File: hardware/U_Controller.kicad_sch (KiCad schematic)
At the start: 14 parts, among them J7001 USB_C_Receptacle_USB2.0_14P, SW7001 SW_Wuerth_450301014042, U7001 STM32C031K6Tx, U7002 STM32C071RBT6, U7003 USBLC6-2SC6, Y7001 Crystal_GND24

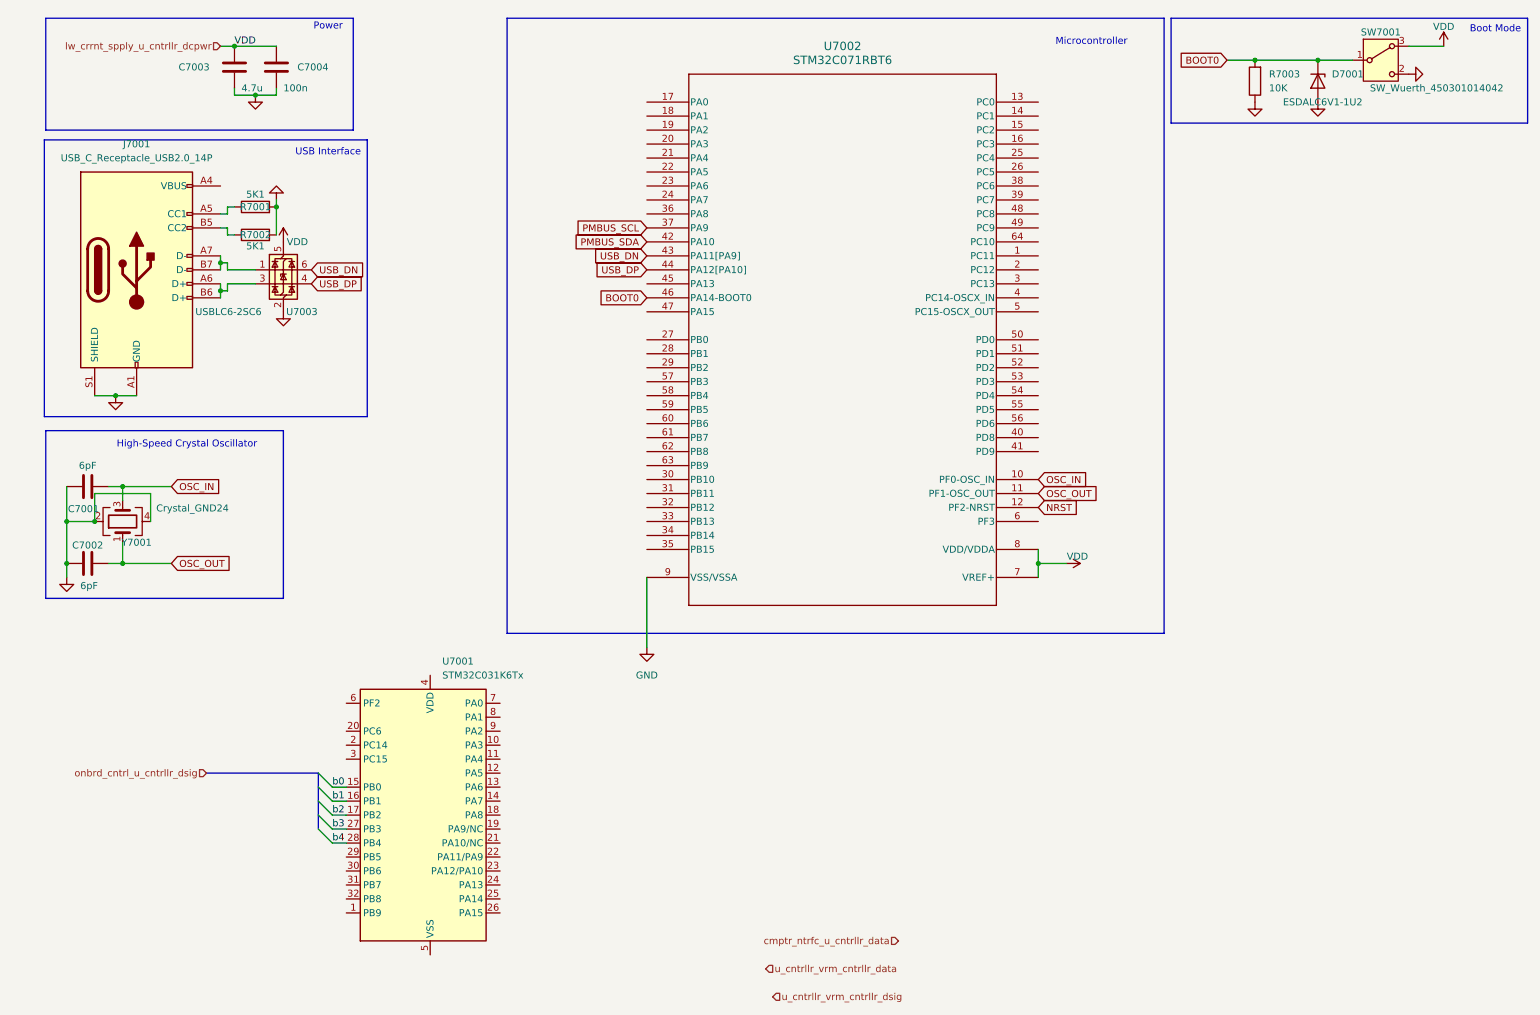
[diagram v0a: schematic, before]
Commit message: refactor(schematic): proper pin mappings
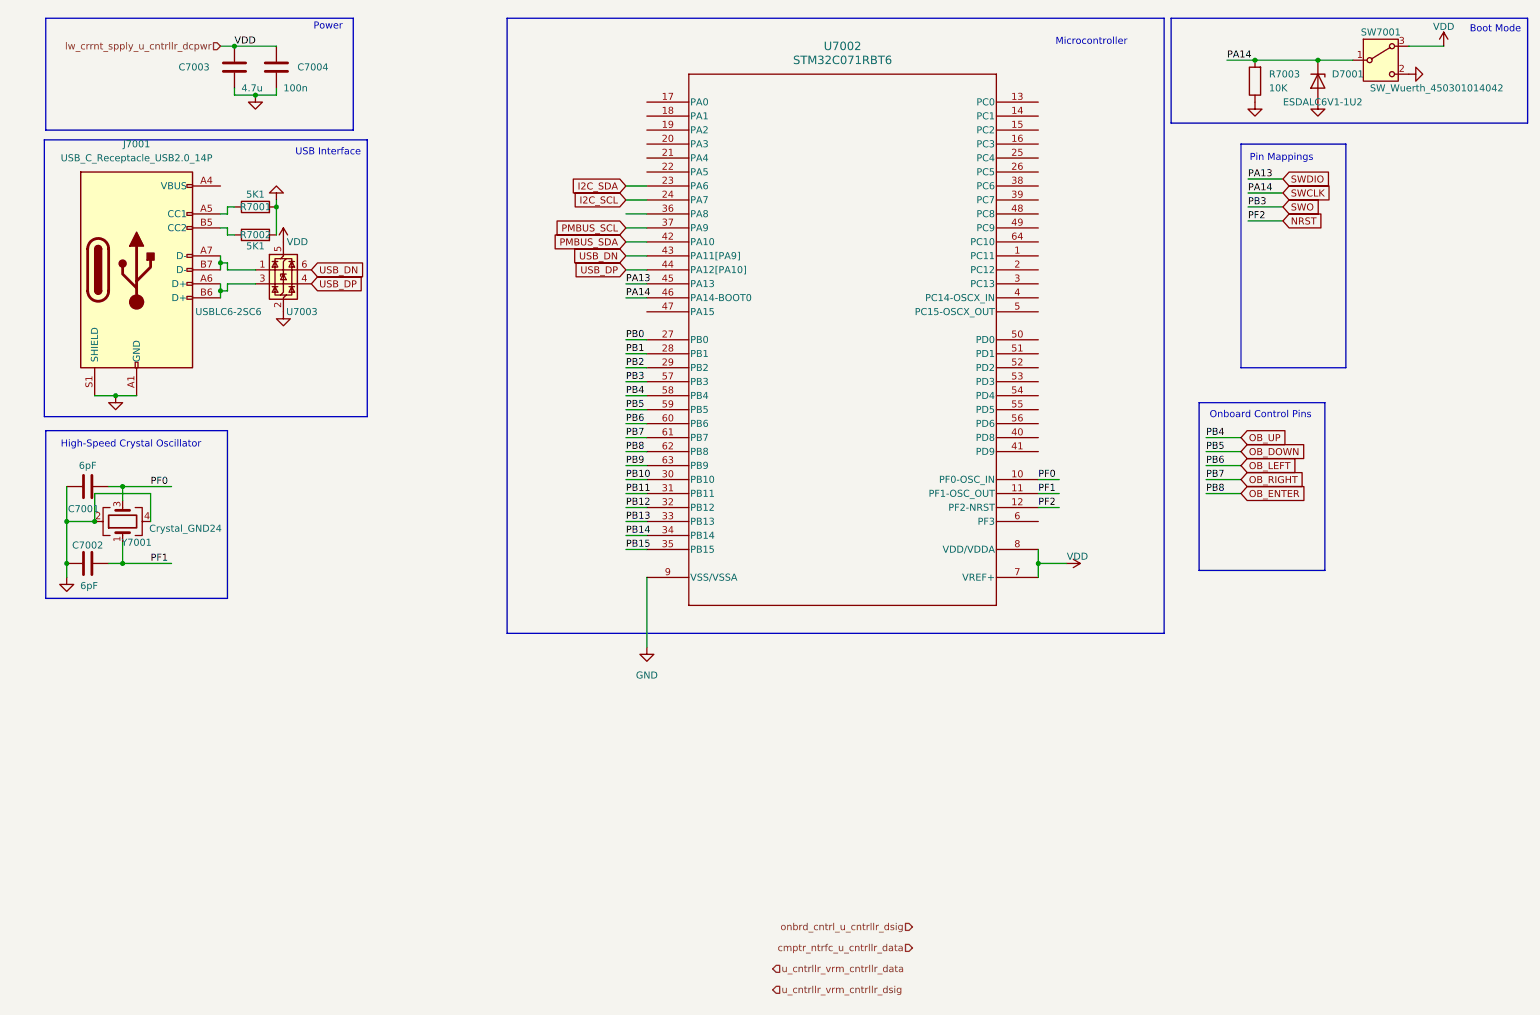
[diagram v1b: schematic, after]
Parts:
- removed U7001: STM32C031K6Tx, Package_QFP:LQFP-32_7x7mm_P0.8mm, symbol MCU_ST_STM32C0:STM32C031K6Tx
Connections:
- net I2C_SDA: now reaches U7002.23 (PA6)
- net I2C_SCL: now reaches U7002.24 (PA7)
- net PB0: now reaches U7002.27 (PB0)
- net PB1: now reaches U7002.28 (PB1)
- net PB2: now reaches U7002.29 (PB2)
- net PB10: now reaches U7002.30 (PB10)
- net PB11: now reaches U7002.31 (PB11)
- net PB12: now reaches U7002.32 (PB12)
- net PB13: now reaches U7002.33 (PB13)
- net PB14: now reaches U7002.34 (PB14)
- net PB15: now reaches U7002.35 (PB15)
- net SWDIO: now reaches U7002.45 (PA13)
- net SWO: now reaches U7002.57 (PB3)
- net OB_UP: now reaches U7002.58 (PB4)
- net OB_DOWN: now reaches U7002.59 (PB5)
- net OB_LEFT: now reaches U7002.60 (PB6)
- net OB_RIGHT: now reaches U7002.61 (PB7)
- net OB_ENTER: now reaches U7002.62 (PB8)
- net PB9: now reaches U7002.63 (PB9)
- net BOOT0 renamed SWCLK
- net OSC_IN renamed PF0
- net OSC_OUT renamed PF1
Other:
- note added: "Onboard Control Pins"
- note added: "Pin Mappings"

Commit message: feat(schematic): SWD connector
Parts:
- added J7002: Conn_ARM_JTAG_SWD_10, symbol Connector:Conn_ARM_JTAG_SWD_10
- added R7004, R7005: 100k, symbol Device:R
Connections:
- net GND: now also J7002.3 (GND), J7002.5 (GND), J7002.9 (GNDDetect), R7005.2
- net NRST: now also J7002.10 (~{RESET})
- net SWCLK: now also J7002.2 (SWDIO/TMS), R7005.1
- net SWDIO: now also J7002.4 (SWCLK/TCK), R7004.2
- net SWO: now also J7002.6 (SWO/TDO)
- net VDD: now also J7002.1 (VTref), R7004.1
- net 12V_CUR_SENS: now reaches U7002.17 (PA0)
- net 12V_VOL_SENS: now reaches U7002.18 (PA1)
- no-connect marks 0 -> 1
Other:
- note added: "12V Supply Pins"
- note added: "SWD Connector"

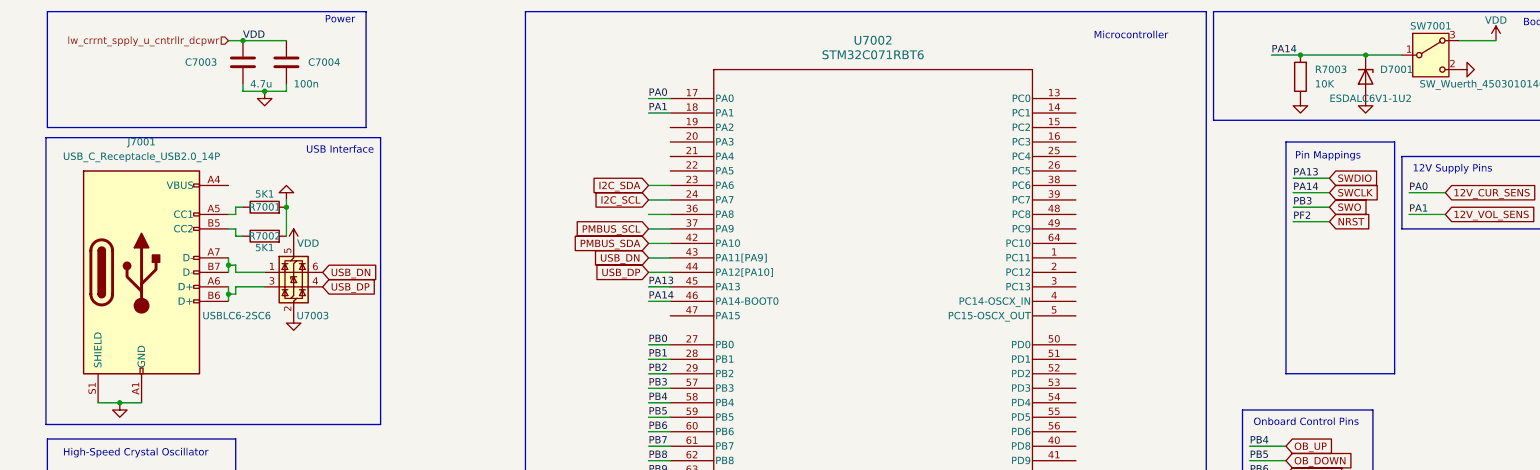
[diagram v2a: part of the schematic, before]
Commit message: chore(schematic): add footprints and datasheets for microcontroller
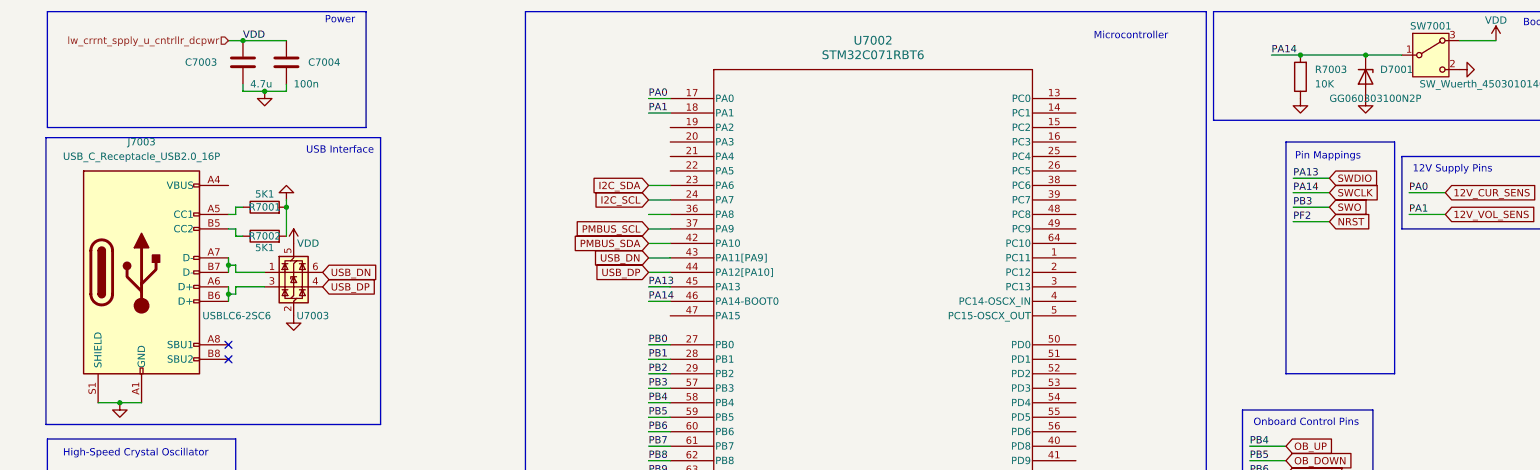
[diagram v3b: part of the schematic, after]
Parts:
- removed J7001: USB_C_Receptacle_USB2.0_14P, symbol Connector:USB_C_Receptacle_USB2.0_14P
- added J7003: USB_C_Receptacle_USB2.0_16P, work:12402012E212A_AMP, symbol Connector:USB_C_Receptacle_USB2.0_16P
- C7001, C7002, C7003, C7004: footprint (none) -> Capacitor_SMD:C_0805_2012Metric
- D7001: value ESDALC6V1-1U2 -> GG060303100N2P; footprint (none) -> Diode_SMD:D_0603_1608Metric
- J7002: footprint (none) -> work:CNC_3221-10-0100-00
- R7001, R7002, R7003, R7004, R7005: footprint (none) -> Resistor_SMD:R_0805_2012Metric
- Y7001: footprint (none) -> Crystal:Crystal_SMD_Abracon_ABM10-4Pin_2.5x2.0mm
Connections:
- net GND: now also J7003.A1 (GND), J7003.A12 (GND), J7003.B1 (GND), J7003.B12 (GND), J7003.S1 (SHIELD)
- net at R7002.1: now also J7003.B5 (CC2)
- net at R7001.1: now also J7003.A5 (CC1)
- net at U7003.3 (I/O2): now also J7003.A6 (D+), J7003.B6 (D+)
- net at U7003.1 (I/O1): now also J7003.A7 (D-), J7003.B7 (D-)
- new net: J7003.A4 (VBUS), J7003.A9 (VBUS), J7003.B4 (VBUS), J7003.B9 (VBUS)
- no-connect marks 1 -> 3
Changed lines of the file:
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@@
 	)
 	(no_connect
+		(at 45.72 72.39)
+	)
+	(no_connect
 		(at 248.92 142.24)
 	)
+	(no_connect
+		(at 45.72 74.93)
+	)
 	(wire
 		(pts
@@
 			)
 		)
-		(property "Footprint" ""
+		(property "Footprint" "Crystal:Crystal_SMD_Abracon_ABM10-4Pin_2.5x2.0mm"
 			(at 27.94 105.41 0)
 			(effects
@@
 			)
 		)
-		(property "Datasheet" "~"
+		(property "Datasheet" "https://www.digikey.com/en/products/detail/abracon-llc/ABM10W-48-0000MHZ-7-D1X-T3/7172572"
 			(at 27.94 105.41 0)
 			(effects
@@
 			)
 		)
-		(property "Footprint" ""
+		(property "Footprint" "Capacitor_SMD:C_0805_2012Metric"
 			(at 25.4 98.0948 0)
 			(effects
@@
 			)
 		)
-		(property "Value" "ESDALC6V1-1U2"
+		(property "Value" "GG060303100N2P"
 			(at 238.76 29.21 90)
 			(effects
@@
 			)
 		)
-		(property "Footprint" ""
+		(property "Footprint" "Diode_SMD:D_0603_1608Metric"
 			(at 245.11 25.4 0)
 			(effects
@@
 			)
 		)
-		(property "Datasheet" "~"
+		(property "Datasheet" "https://www.digikey.com/en/products/detail/kyocera-avx/GG060303100N2P/22245452?s=N4IgjCBcpgbFoDGUBmBDANgZwKYBoQB7KAbRAGYBOAJgBZ4BdAgBwBcoQBlVgJwEsAdgHMQAXwIB2WBGghkkdNnxFS4CbTBgArCCYg2Hbv2FjRooA"
 			(at 245.11 25.4 0)
 			(effects
@@
 			)
 		)
-		(property "Description" "Zener diode"
+		(property "Description" "TVS Zener diode"
 			(at 245.11 25.4 0)
 			(effects
@@
 			)
 		)
-		(property "Footprint" ""
+		(property "Footprint" "Capacitor_SMD:C_0805_2012Metric"
 			(at 49.2252 26.67 0)
 			(effects
@@
 			)
 		)
-		(property "Footprint" ""
+		(property "Footprint" "Capacitor_SMD:C_0805_2012Metric"
 			(at 25.4 112.0648 0)
 			(effects
@@
 			)
 		)
-		(property "Footprint" ""
+		(property "Footprint" "Resistor_SMD:R_0805_2012Metric"
 			(at 235.458 25.4 90)
 			(effects
@@
 			)
 		)
-		(property "Footprint" ""
+		(property "Footprint" "Capacitor_SMD:C_0805_2012Metric"
 			(at 56.8452 26.67 0)
 			(effects
@@
 			)
 		)
-		(property "Footprint" ""
+		(property "Footprint" "Resistor_SMD:R_0805_2012Metric"
 			(at 52.07 55.118 90)
 			(effects
@@
 	)
 	(symbol
-		(lib_id "Connector:USB_C_Receptacle_USB2.0_14P")
-		(at 30.48 59.69 0)
-		(unit 1)
-		(exclude_from_sim no)
-		(in_bom yes)
-		(on_board yes)
-		(dnp no)
-		(fields_autoplaced yes)
-		(property "Reference" "J7001"
-			(at 30.48 36.83 0)
-			(effects
-				(font
-					(size 1.27 1.27)
-				)
-			)
-		)
-		(property "Value" "USB_C_Receptacle_USB2.0_14P"
-			(at 30.48 39.37 0)
-			(effects
-				(font
-					(size 1.27 1.27)
-				)
-			)
-		)
-		(property "Footprint" ""
-			(at 34.29 59.69 0)
-			(effects
-				(font
-					(size 1.27 1.27)
-				)
-				(hide yes)
-			)
-		)
-		(property "Datasheet" "https://www.usb.org/sites/default/files/documents/usb_type-c.zip"
-			(at 34.29 59.69 0)
-			(effects
-				(font
-					(size 1.27 1.27)
-				)
-				(hide yes)
-			)
-		)
-		(property "Description" "USB 2.0-only 14P Type-C Receptacle connector"
-			(at 30.48 59.69 0)
-			(effects
-				(font
-					(size 1.27 1.27)
-				)
-				(hide yes)
-			)
-		)
-		(pin "B12"
-		)
-		(pin "B6"
-		)
-		(pin "B9"
-		)
-		(pin "A1"
-		)
-		(pin "B7"
-		)
-		(pin "B4"
-		)
-		(pin "S1"
-		)
-		(pin "B1"
-		)
-		(pin "B5"
-		)
-		(pin "A12"
-		)
-		(pin "A4"
-		)
-		(pin "A5"
-		)
-		(pin "A6"
-		)
-		(pin "A7"
-		)
-		(pin "A9"
-		)
-		(instances
-			(project ""
-				(path "/d5303413-7068-41ba-88e3-39dfa38d31b7/027ff087-ab1d-45e5-9d8f-c94102656fe5"
-					(reference "J7001")
-					(unit 1)
-				)
-			)
-		)
-	)
-	(symbol
 		(lib_id "power:VDD")
 		(at 236.22 121.92 0)
@@
 			)
 		)
-		(property "Footprint" ""
+		(property "Footprint" "Resistor_SMD:R_0805_2012Metric"
 			(at 52.07 50.038 90)
 			(effects
@@
 			)
 		)
-		(property "Footprint" ""
+		(property "Footprint" "Resistor_SMD:R_0805_2012Metric"
 			(at 256.032 148.59 90)
 			(effects
@@
 	)
 	(symbol
+		(lib_id "Connector:USB_C_Receptacle_USB2.0_16P")
+		(at 30.48 59.69 0)
+		(unit 1)
+		(exclude_from_sim no)
+		(in_bom yes)
+		(on_board yes)
+		(dnp no)
+		(fields_autoplaced yes)
+		(property "Reference" "J7003"
+			(at 30.48 36.83 0)
+			(effects
+				(font
+					(size 1.27 1.27)
+				)
+			)
+		)
+		(property "Value" "USB_C_Receptacle_USB2.0_16P"
+			(at 30.48 39.37 0)
+			(effects
+				(font
+					(size 1.27 1.27)
+				)
+			)
+		)
+		(property "Footprint" "work:12402012E212A_AMP"
+			(at 34.29 59.69 0)
+			(effects
+				(font
+					(size 1.27 1.27)
+				)
+				(hide yes)
+			)
+		)
+		(property "Datasheet" "https://www.digikey.com/en/products/detail/amphenol-cs-commercial-products/12402012E212A/13683192"
+			(at 34.29 59.69 0)
+			(effects
+				(font
+					(size 1.27 1.27)
+				)
+				(hide yes)
+			)
+		)
+		(property "Description" "USB 2.0-only 16P Type-C Receptacle connector"
+			(at 30.48 59.69 0)
+			(effects
+				(font
+					(size 1.27 1.27)
+				)
+				(hide yes)
+			)
+		)
+		(pin "A9"
+		)
+		(pin "B8"
+		)
+		(pin "B6"
+		)
+		(pin "B7"
+		)
+		(pin "A12"
+		)
+		(pin "B5"
+		)
+		(pin "B12"
+		)
+		(pin "B1"
+		)
+		(pin "S1"
+		)
+		(pin "A4"
+		)
+		(pin "A5"
+		)
+		(pin "A6"
+		)
+		(pin "A7"
+		)
+		(pin "A8"
+		)
+		(pin "B9"
+		)
+		(pin "A1"
+		)
+		(pin "B4"
+		)
+		(instances
+			(project ""
+				(path "/d5303413-7068-41ba-88e3-39dfa38d31b7/027ff087-ab1d-45e5-9d8f-c94102656fe5"
+					(reference "J7003")
+					(unit 1)
+				)
+			)
+		)
+	)
+	(symbol
 		(lib_id "power:GND")
 		(at 57.15 67.31 0)
@@
 			)
 		)
-		(property "Datasheet" "STM32C071RBT6"
+		(property "Datasheet" "https://www.st.com/en/microcontrollers-microprocessors/stm32c071rb.html#documentation"
 			(at 123.19 29.21 0)
 			(effects
@@
 			)
 		)
-		(property "Footprint" ""
+		(property "Footprint" "work:CNC_3221-10-0100-00"
 			(at 236.22 137.16 0)
 			(effects
@@
 			)
 		)
-		(property "Datasheet" "http://infocenter.arm.com/help/topic/com.arm.doc.ddi0314h/DDI0314H_coresight_components_trm.pdf"
+		(property "Datasheet" "https://www.digikey.com/en/products/detail/cnc-tech/3221-10-0100-00/4878932"
 			(at 227.33 168.91 90)
 			(effects
@@
 			)
 		)
-		(property "Footprint" ""
+		(property "Footprint" "Resistor_SMD:R_0805_2012Metric"
 			(at 256.032 125.73 90)
 			(effects
